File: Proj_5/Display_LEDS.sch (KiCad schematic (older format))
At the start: 6 parts, among them J1 DSUB-9, J2 DSUB-9, U27 max235cpg

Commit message: Dont be wonky:
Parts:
- gave numbers to parts that had none: 1
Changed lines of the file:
@@
 P 5800 5350
 AR Path="/5EA98353/5EA6A56C" Ref="C?"  Part="1"
-AR Path="/5EAF7226/5EA6A56C" Ref="C?"  Part="1"
-F 0 "C?" V 5548 5350 50  0000 C CNN
+AR Path="/5EAF7226/5EA6A56C" Ref="C15"  Part="1"
+F 0 "C15" V 5548 5350 50  0000 C CNN
 F 1 "0.1uF" V 5639 5350 50  0000 C CNN
 F 2 "" H 5838 5200 50  0001 C CNN
@@
 	5800 5000 6100 5000
 $Comp
-L power:GND #PWR?
+L power:GND #PWR010
 U 1 1 5EAAD1B7
 P 5800 5500
-F 0 "#PWR?" H 5800 5250 50  0001 C CNN
+F 0 "#PWR010" H 5800 5250 50  0001 C CNN
 F 1 "GND" H 5805 5327 50  0000 C CNN
 F 2 "" H 5800 5500 50  0001 C CNN

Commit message: LCD boop
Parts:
- removed DS2: LCD4x20, LCD4x20, symbol LCD4x20:LCD4x20
- removed J2: DSUB-9, DSUB-9, symbol DSUB-9:DSUB-9
- added U?: PAL16L8, symbol Logic_Programmable:PAL16L8
- added U? (x8): 74LVC1G11, symbol 74xGxx:74LVC1G11
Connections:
- net labels added: +3.3V, +3V0, A0, A1, A10, A11, A12, A13, A14, A15, A16, A17, A18, A19, A2, A3, A4, A5, A6, A7, A8, A9, D0, D1, D2, D3, D4, D5, D6, D7, RS, R~W
- wire segments 2 -> 119
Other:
- moved on the sheet: C15, DS1, J1, U27

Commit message: Rerouted Ext Wires, UART Mostly Complete, All Headers Added
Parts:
- removed C15: 0.1uF, symbol Device:C
- removed J1: DSUB-9, DSUB-9, symbol DSUB-9:DSUB-9
- removed U27: max235cpg, max235cpg, symbol max235cpg:max235cpg
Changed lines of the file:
@@
 $Descr A2 23386 16535
 encoding utf-8
-Sheet 5 9
+Sheet 4 9
 Title ""
 Date ""
@@
 F 8 "Newhaven Display" H 12450 1600 50  0001 L CNN "Manufacturer_Name"
 	1    11500 2100
-	1    0    0    -1
-$EndComp
-$Comp
-L DSUB-9:DSUB-9 J1
-U 1 1 5EAFF563
-P 12600 8700
-F 0 "J1" H 13428 8353 60  0000 L CNN
-F 1 "DSUB-9" H 13428 8247 60  0000 L CNN
-F 2 "DSUB-9" H 13200 8340 60  0001 C CNN
-F 3 "" H 12600 8700 60  0000 C CNN
-	1    12600 8700
-	1    0    0    -1
-$EndComp
-$Comp
-L max235cpg:max235cpg U27
-U 1 1 5F18FC44
-P 8650 8700
-F 0 "U27" H 9950 9087 60  0000 C CNN
-F 1 "max235cpg" H 9950 8981 60  0000 C CNN
-F 2 "max235cpg" H 9950 8940 60  0001 C CNN
-F 3 "" H 8650 8700 60  0000 C CNN
-	1    8650 8700
-	1    0    0    -1
-$EndComp
-$Comp
-L Device:C C?
-U 1 1 5EA6A56C
-P 8350 10150
-AR Path="/5EA98353/5EA6A56C" Ref="C?"  Part="1"
-AR Path="/5EAF7226/5EA6A56C" Ref="C15"  Part="1"
-F 0 "C15" V 8098 10150 50  0000 C CNN
-F 1 "0.1uF" V 8189 10150 50  0000 C CNN
-F 2 "" H 8388 10000 50  0001 C CNN
-F 3 "~" H 8350 10150 50  0001 C CNN
-	1    8350 10150
-	1    0    0    -1
-$EndComp
-Wire Wire Line
-	8350 10000 8350 9800
-Wire Wire Line
-	8350 9800 8650 9800
-$Comp
-L power:GND #PWR010
-U 1 1 5EAAD1B7
-P 8350 10300
-F 0 "#PWR010" H 8350 10050 50  0001 C CNN
-F 1 "GND" H 8355 10127 50  0000 C CNN
-F 2 "" H 8350 10300 50  0001 C CNN
-F 3 "" H 8350 10300 50  0001 C CNN
-	1    8350 10300
 	1    0    0    -1
 $EndComp
@@
 	0    -1   -1   0
 $EndComp
-Wire Bus Line
-	1500 600  12300 600
-Wire Bus Line
-	1500 15000 12350 15000
-Wire Bus Line
-	1500 600  1500 15000
 $Comp
 L power:GND #PWR?
@@
 	0    1    1    0
 $EndComp
+Wire Bus Line
+	1500 600  12300 600
+Wire Bus Line
+	1500 15000 12350 15000
+Wire Bus Line
+	1500 600  1500 15000
 $EndSCHEMATC

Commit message: Monch
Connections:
- net at U?.12 (IO8): now also DS1.6 (E)
- net at U?.19 (IO1): no longer DS1.6 (E)
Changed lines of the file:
@@
 	11500 2600 9350 2600
-Wire Wire Line
-	9350 2600 9350 2100
-Wire Wire Line
-	9350 2100 8950 2100
 Wire Wire Line
 	11500 2500 10250 2500
@@
 	0    1    1    0
 $EndComp
+Wire Wire Line
+	9350 2600 9350 2800
+Wire Wire Line
+	9350 2800 8950 2800
 Wire Bus Line
 	1500 600  12300 600

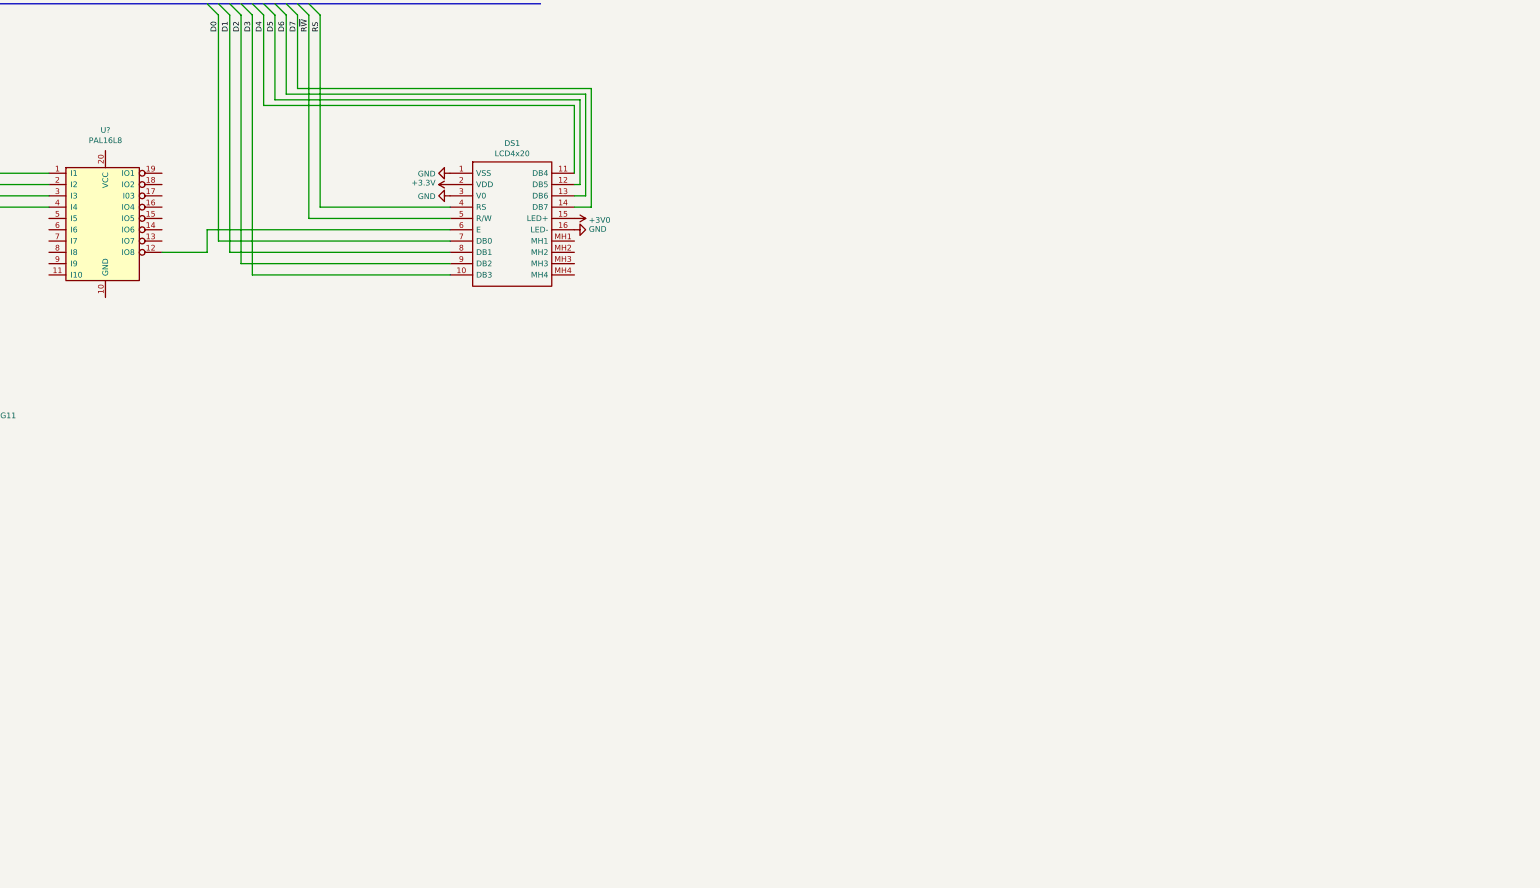
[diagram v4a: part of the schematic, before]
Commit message: Remaining LED Components Added, Final pins added to headers.
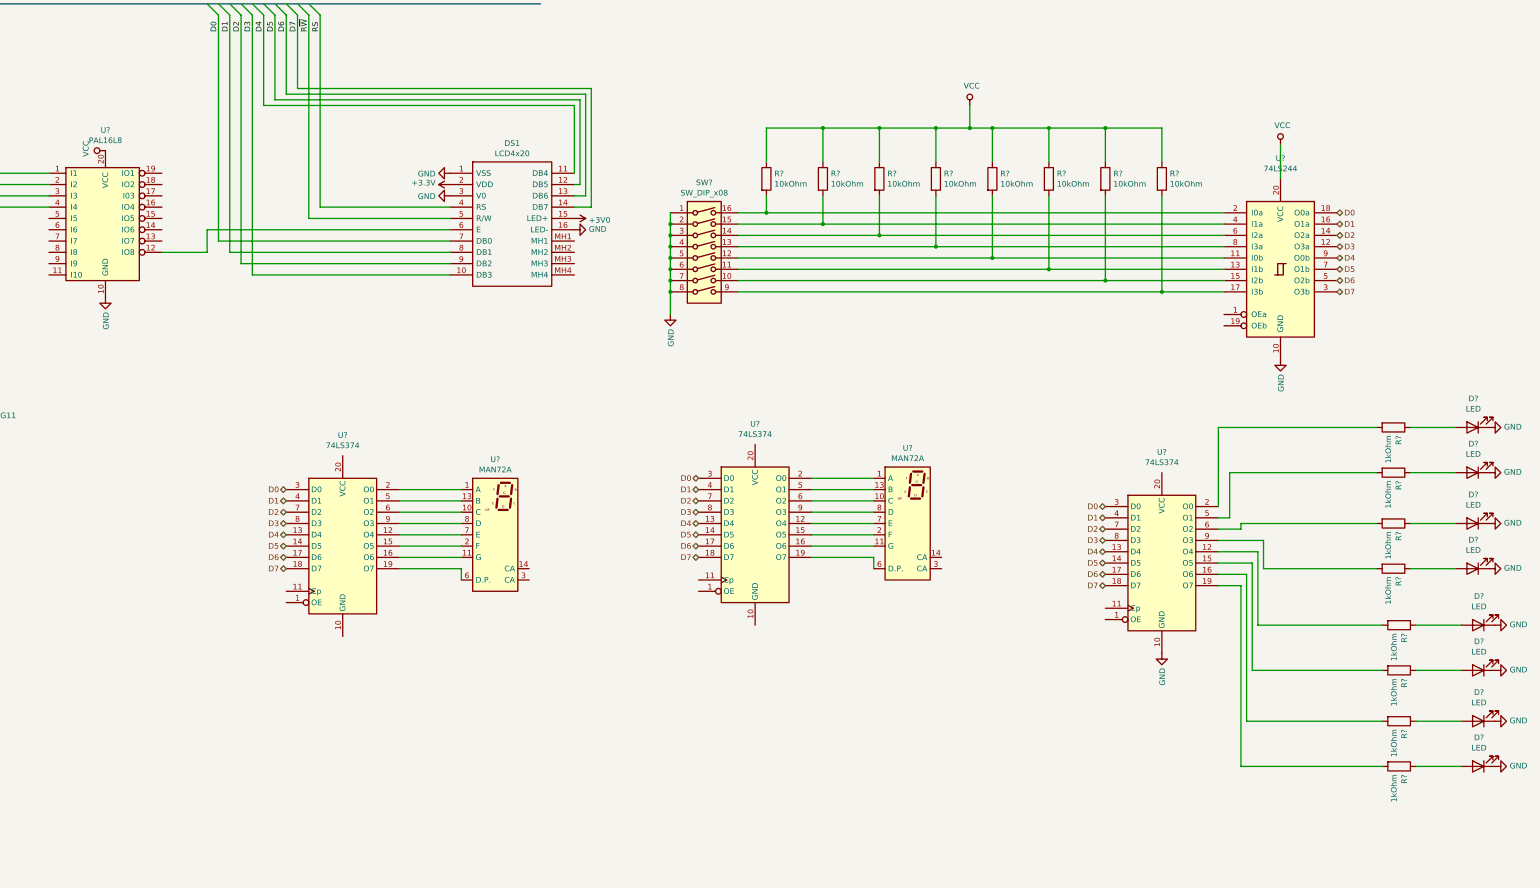
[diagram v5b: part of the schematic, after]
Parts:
- added D? (x8): LED, symbol Device:LED
- added R? (x8): 10kOhm, symbol Device:R
- added R? (x8): 1kOhm, symbol Device:R
- added SW?: SW_DIP_x08, symbol Switch:SW_DIP_x08
- added U?: 74LS244, symbol 74xx:74LS244
- added U? (x2): MAN72A, Display_7Segment:MAN72A, symbol Display_Character:MAN72A
- added U? (x3): 74LS374, symbol 74xx:74LS374
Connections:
- net D0: now also U?.18 (O0a), U?.3 (D0), U?.3 (D0), U?.3 (D0)
- net D1: now also U?.16 (O1a), U?.4 (D1), U?.4 (D1), U?.4 (D1)
- net D2: now also U?.14 (O2a), U?.7 (D2), U?.7 (D2), U?.7 (D2)
- net D3: now also U?.12 (O3a), U?.8 (D3), U?.8 (D3), U?.8 (D3)
- net D4: now also U?.13 (D4), U?.13 (D4), U?.13 (D4), U?.9 (O0b)
- net D5: now also U?.14 (D5), U?.14 (D5), U?.14 (D5), U?.7 (O1b)
- net D6: now also U?.17 (D6), U?.17 (D6), U?.17 (D6), U?.5 (O2b)
- net D7: now also U?.18 (D7), U?.18 (D7), U?.18 (D7), U?.3 (O3b)
- net GND: now also U?.10 (GND), D?.1 (K), D?.1 (K), D?.1 (K), D?.1 (K), D?.1 (K), D?.1 (K), D?.1 (K), D?.1 (K), SW?.1, SW?.2, SW?.3, SW?.4, SW?.5, SW?.6, SW?.7, SW?.8, U?.10 (GND), U?.10 (GND)
- net VCC: now also U?.20 (VCC), R?.1, R?.1, R?.1, R?.1, R?.1, R?.1, R?.1, R?.1, U?.20 (VCC)
- new net: R?.2, SW?.12, U?.11 (I0b)
- new net: R?.2, SW?.11, U?.13 (I1b)
- new net: R?.2, SW?.10, U?.15 (I2b)
- new net: R?.2, SW?.9, U?.17 (I3b)
- new net: R?.2, SW?.16, U?.2 (I0a)
- new net: R?.2, SW?.15, U?.4 (I1a)
- new net: R?.2, SW?.14, U?.6 (I2a)
- new net: R?.2, SW?.13, U?.8 (I3a)
- new net: U?.1 (A), U?.2 (O0) (x2)
- new net: U?.10 (C), U?.6 (O2) (x2)
- new net: U?.11 (G), U?.16 (O6) (x2)
- new net: U?.13 (B), U?.5 (O1) (x2)
- new net: U?.15 (O5), U?.2 (F) (x2)
- new net: U?.19 (O7), U?.6 (D.P.) (x2)
- new net: U?.12 (O4), U?.7 (E) (x2)
- new net: U?.8 (D), U?.9 (O3) (x2)
- new net: R?.2, U?.12 (O4)
- new net: R?.2, U?.15 (O5)
- new net: R?.2, U?.16 (O6)
- new net: R?.2, U?.19 (O7)
- new net: R?.2, U?.2 (O0)
- new net: R?.2, U?.5 (O1)
- new net: R?.2, U?.6 (O2)
- new net: R?.2, U?.9 (O3)
- new net: D?.2 (A), R?.1 (x8)

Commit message: Added Power Flags, finished no connects.
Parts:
- removed D? (x4): LED, symbol Device:LED
- added D5, D6, D7, D8: LED, symbol Device:LED
- gave numbers to parts that had none: 36
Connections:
- net GND: now also U33.10 (GND), U35.10 (GND), D5.1 (K), D6.1 (K), D7.1 (K), D8.1 (K)
- net VCC: now also U33.20 (VCC), U35.20 (VCC), U37.20 (VCC)
- net at R13.1: now also D5.2 (A)
- net at R14.1: now also D6.2 (A)
- net at R15.1: now also D7.2 (A)
- net at R16.1: now also D8.2 (A)

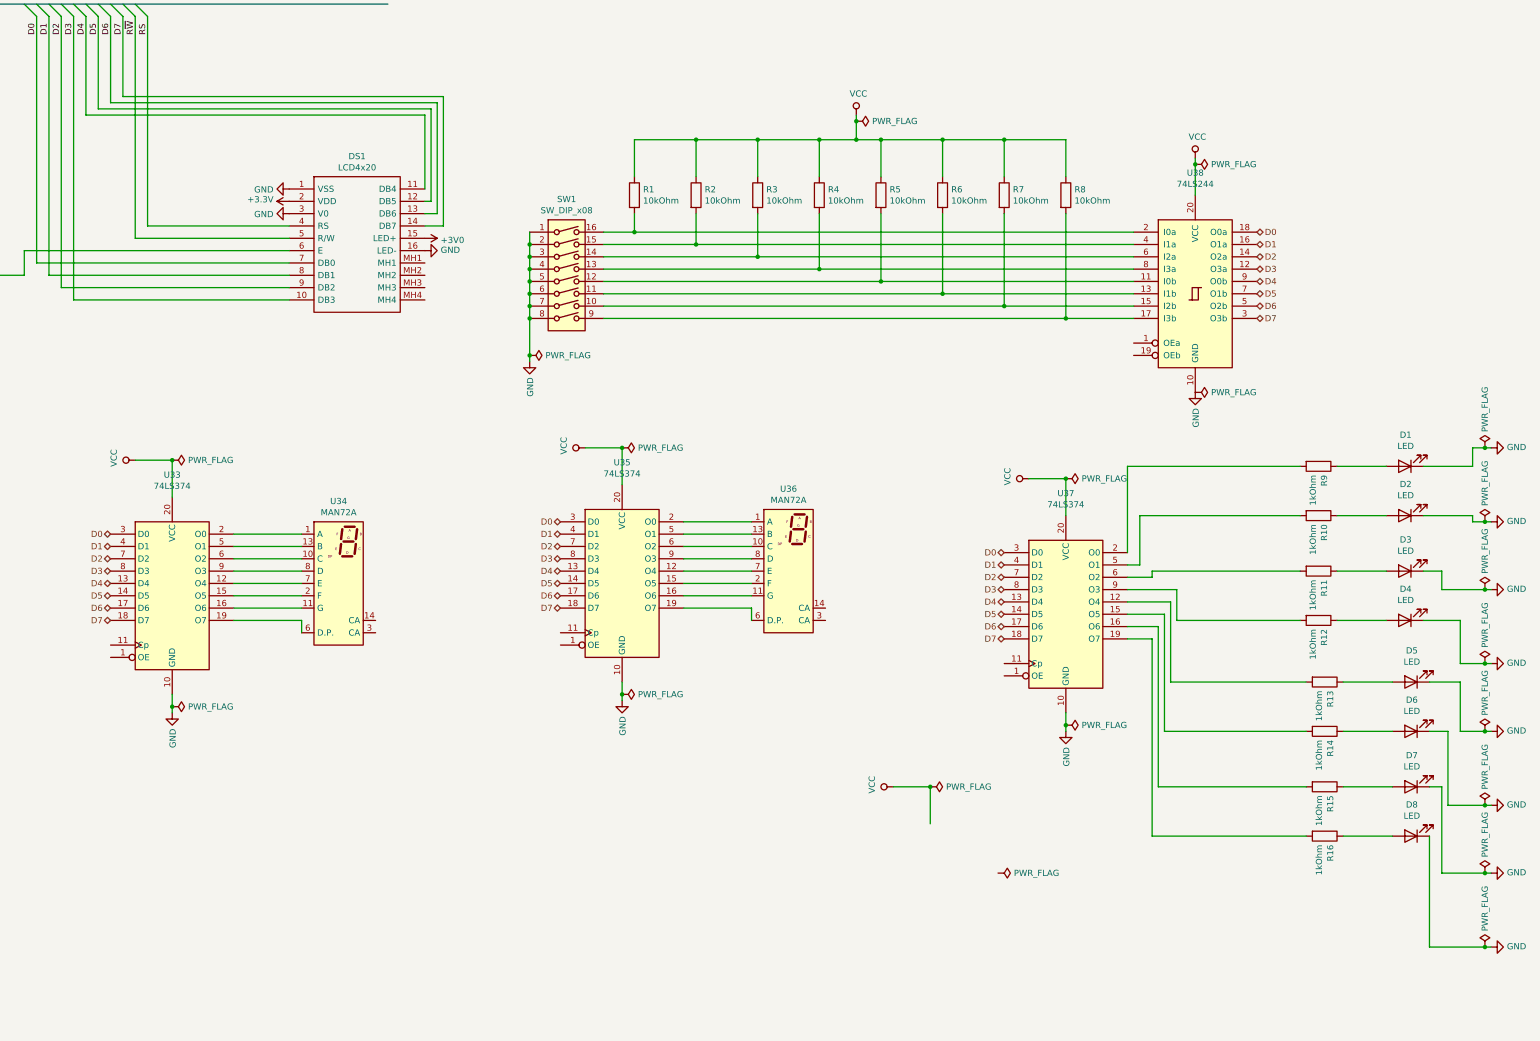
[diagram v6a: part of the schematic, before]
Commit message: Finished Most of power flags, power connector header, added hierachical pins to a few sheets.
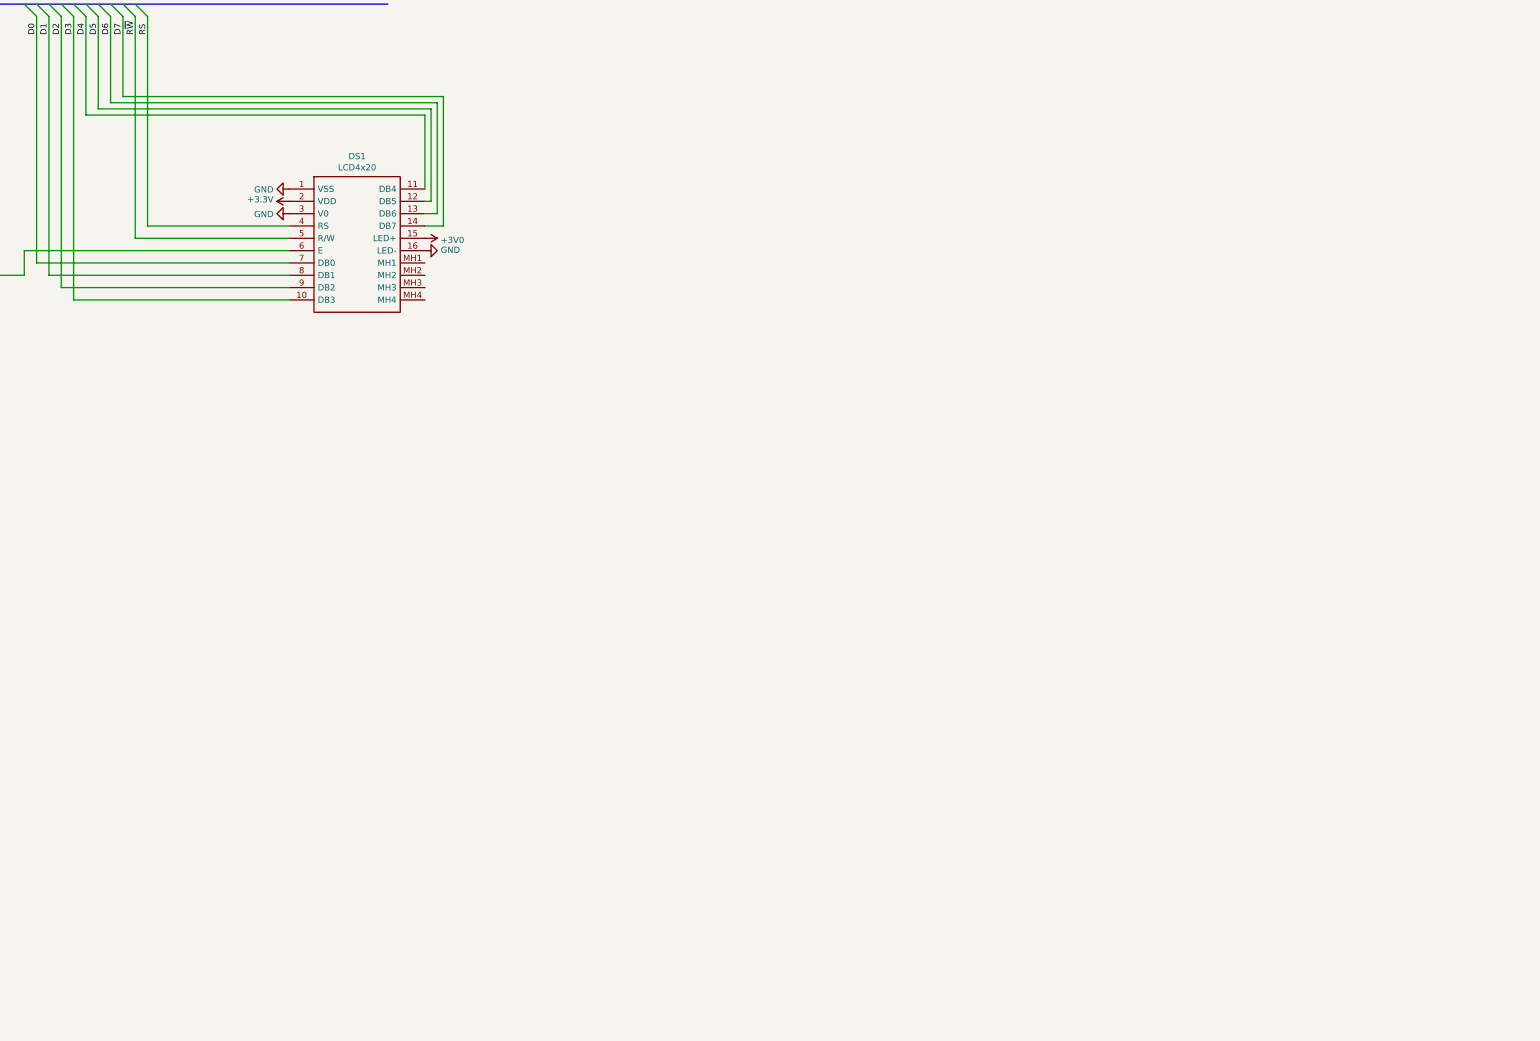
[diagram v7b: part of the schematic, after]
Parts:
- removed D1, D2, D3, D4, D5, D6, D7, D8: LED, symbol Device:LED
- removed R1, R2, R3, R4, R5, R6, R7, R8: 10kOhm, symbol Device:R
- removed R10, R11, R12, R13, R14, R15, R16, R9: 1kOhm, symbol Device:R
- removed SW1: SW_DIP_x08, symbol Switch:SW_DIP_x08
- removed U33, U35, U37: 74LS374, symbol 74xx:74LS374
- removed U34, U36: MAN72A, Display_7Segment:MAN72A, symbol Display_Character:MAN72A
- removed U38: 74LS244, symbol 74xx:74LS244

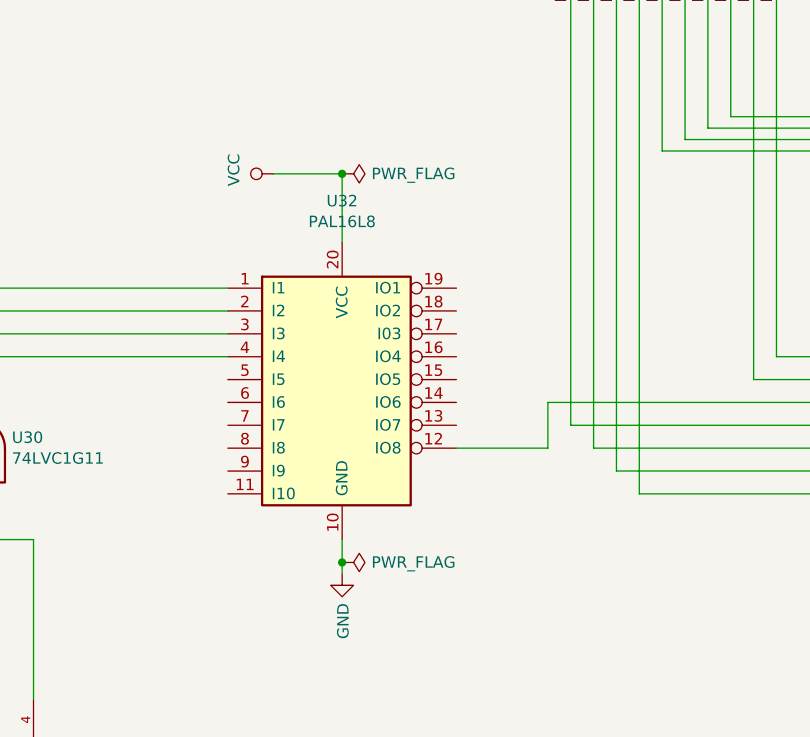
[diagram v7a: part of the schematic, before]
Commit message: Power Flags
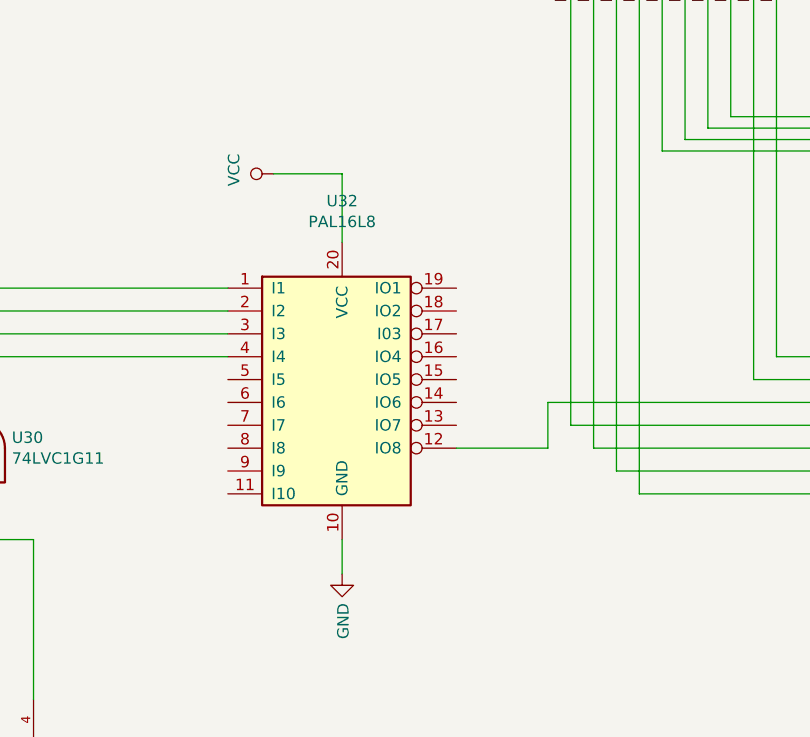
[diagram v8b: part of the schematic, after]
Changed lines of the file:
@@
 Wire Wire Line
 	9350 2600 9350 2800
-$Comp
-L power:PWR_FLAG #FLG019
-U 1 1 5EB3044F
-P 8450 1600
-F 0 "#FLG019" H 8450 1675 50  0001 C CNN
-F 1 "PWR_FLAG" V 8450 1728 50  0000 L CNN
-F 2 "" H 8450 1600 50  0001 C CNN
-F 3 "~" H 8450 1600 50  0001 C CNN
-	1    8450 1600
-	0    1    1    0
-$EndComp
 Wire Wire Line
 	6850 2400 7950 2400
@@
 Wire Wire Line
 	8450 1600 8450 1900
-Connection ~ 8450 1600
 $Comp
 L power:GND #PWR021
@@
 	1    0    0    -1
 $EndComp
-$Comp
-L power:PWR_FLAG #FLG020
-U 1 1 5EC12844
-P 8450 3300
-F 0 "#FLG020" H 8450 3375 50  0001 C CNN
-F 1 "PWR_FLAG" V 8450 3428 50  0000 L CNN
-F 2 "" H 8450 3300 50  0001 C CNN
-F 3 "~" H 8450 3300 50  0001 C CNN
-	1    8450 3300
-	0    1    1    0
-$EndComp
 Wire Wire Line
-	8450 3200 8450 3300
-Connection ~ 8450 3300
-Wire Wire Line
-	8450 3300 8450 3350
+	8450 3200 8450 3350
 Wire Bus Line
 	1500 600  12300 600
